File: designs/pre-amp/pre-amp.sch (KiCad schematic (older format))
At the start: 27 parts, among them J1 Conn_Coaxial, J2 Conn_01x03, J3 Conn_Coaxial, U1 AD8429, U2 OPA211

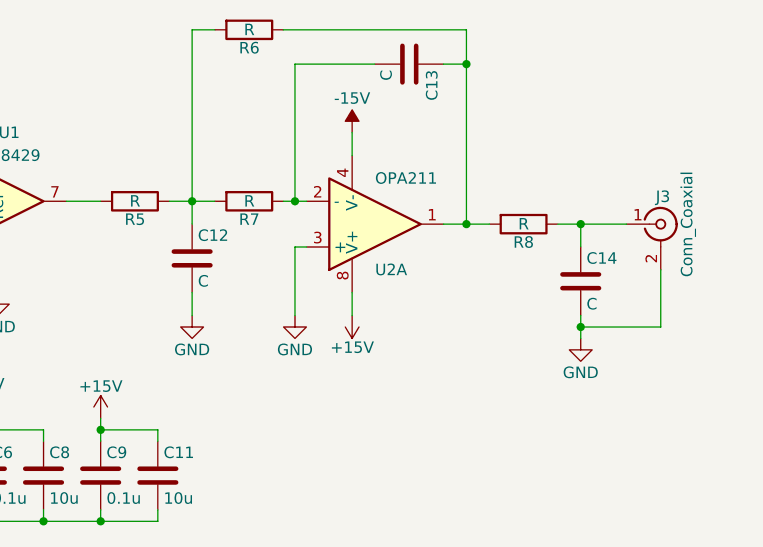
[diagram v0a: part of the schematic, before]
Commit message: [designs/pre-amp] layout
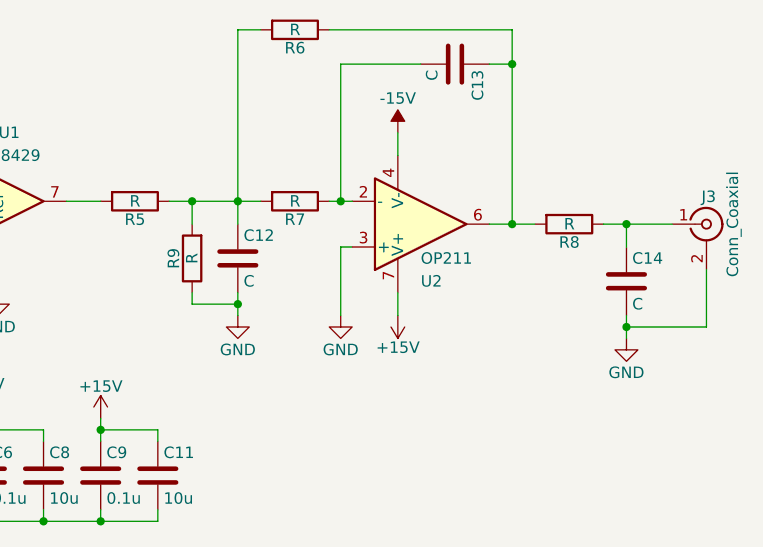
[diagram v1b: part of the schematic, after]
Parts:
- removed U2: OPA211, Housings_SOIC:SOIC-8_3.9x4.9mm_Pitch1.27mm, symbol OPA2134
- added R9: R, Resistors_SMD:R_0603, symbol R
- added U2: OP211, Housings_SOIC:SOIC-8_3.9x4.9mm_Pitch1.27mm, symbol OP179GS
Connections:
- net +15V: now also U2.7 (V+)
- net -15V: now also U2.4 (V-)
- net GND: now also R9.1, U2.3 (+)
- net at C12.1, R5.1, R6.2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: now also R9.2
- net at C13.2, R7.1: now also U2.2 (-)
- net at C13.1, R6.1, R8.2: now also U2.6
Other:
- moved on the sheet: C12, C13, C14, J3, R6, R7, R8

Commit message: [designs/pre-amp] value selections
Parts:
- C14: value C -> 0
- R8: value R -> 0
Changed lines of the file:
@@
 P 5000 1600
 F 0 "R8" V 5080 1600 50  0000 C CNN
-F 1 "R" V 5000 1600 50  0000 C CNN
+F 1 "0" V 5000 1600 50  0000 C CNN
 F 2 "Resistors_SMD:R_0603" V 4930 1600 50  0001 C CNN
 F 3 "" H 5000 1600 50  0001 C CNN
@@
 P 5250 1850
 F 0 "C14" H 5275 1950 50  0000 L CNN
-F 1 "C" H 5275 1750 50  0000 L CNN
+F 1 "0" H 5275 1750 50  0000 L CNN
 F 2 "Capacitors_SMD:C_0603" H 5288 1700 50  0001 C CNN
 F 3 "" H 5250 1850 50  0001 C CNN

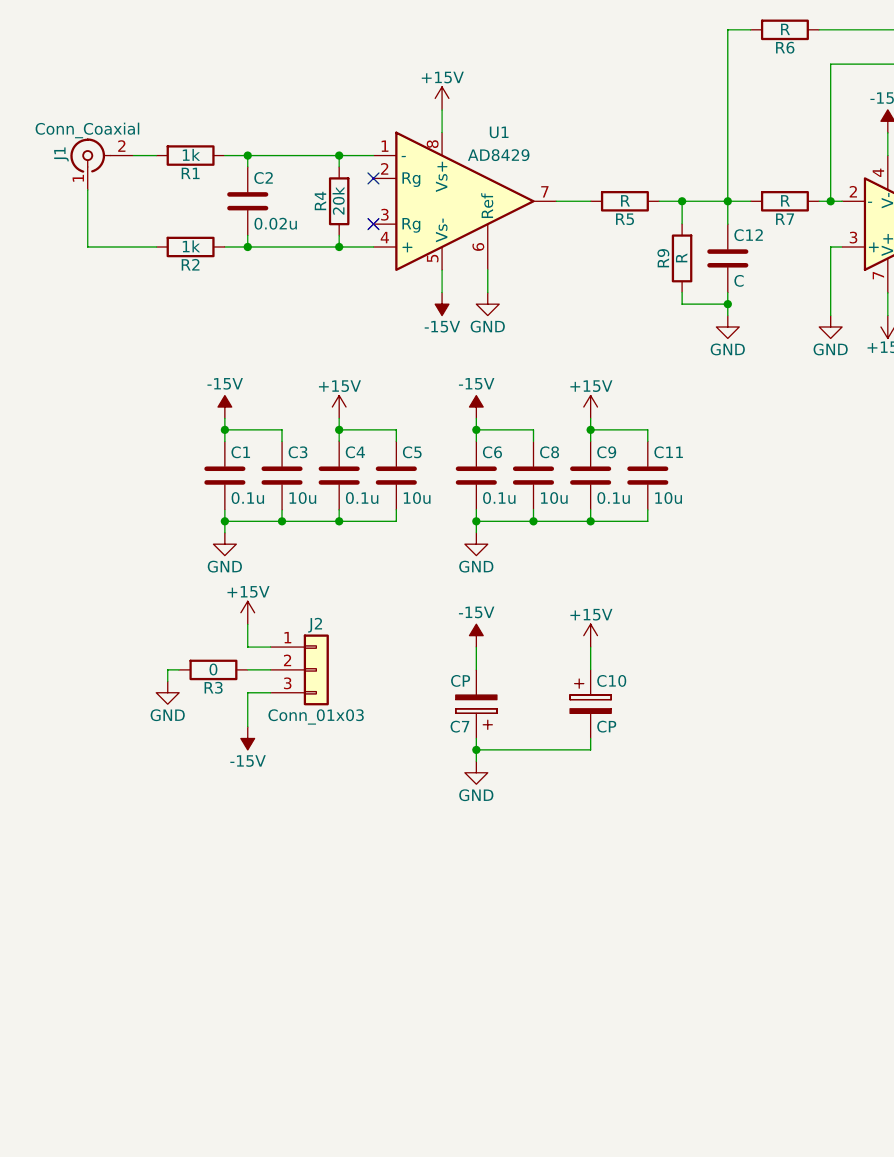
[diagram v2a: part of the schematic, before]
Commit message: [designs/pre-amp] new layout
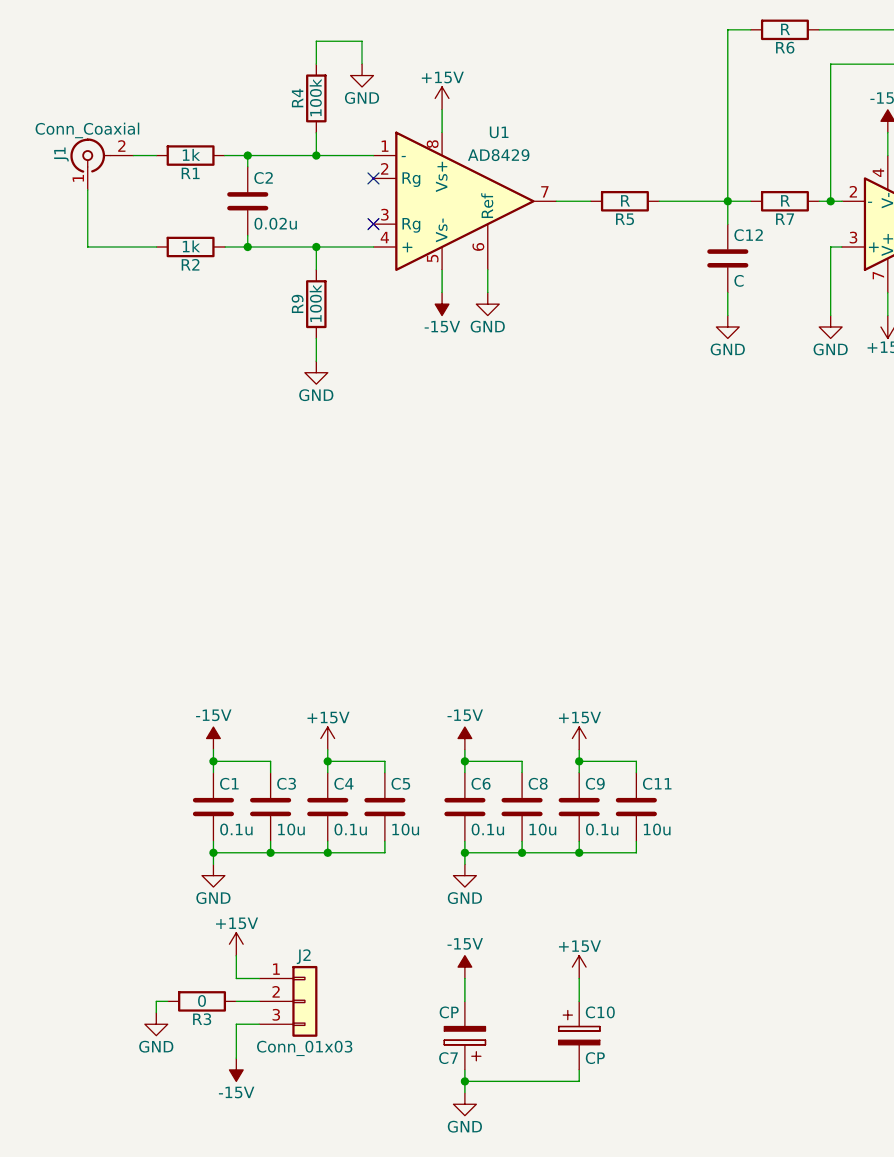
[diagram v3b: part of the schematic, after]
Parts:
- J1, J3: footprint Connectors_TE-Connectivity:BNC_Socket_TYCO-AMP_LargePads -> Connectors2:BNC_Socket_Right-Angle_LargePads
- R4: value 20k -> 100k
- R9: value R -> 100k
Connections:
- net GND: now also R4.2
- net at C2.1, R1.1, U1.1 (-): now also R4.1; no longer R4.2
- net at C2.2, R2.1, U1.4 (+): now also R9.2; no longer R4.1
- net at C12.1, R5.1, R6.2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: no longer R9.2
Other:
- moved on the sheet: C1, C10, C11, C3, C4, C5, C6, C7, C8, C9, J2, R3

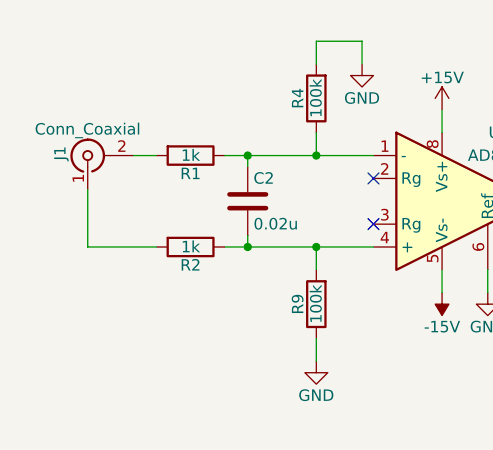
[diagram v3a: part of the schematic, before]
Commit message: [designs/pre-amp] flip input and tweak connection near the edges
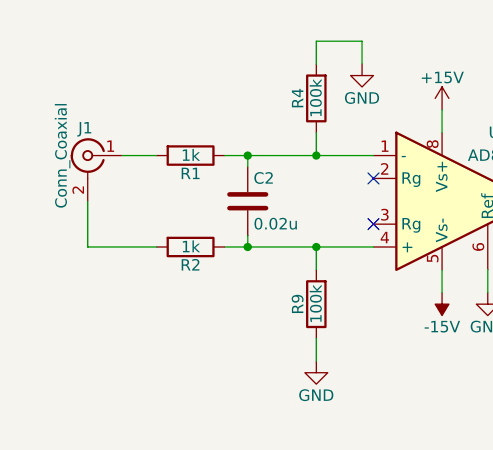
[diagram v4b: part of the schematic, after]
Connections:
- net at J1.1 (In): now also R1.2; no longer R2.2
- net at J1.2 (Ext): now also R2.2; no longer R1.2
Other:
- moved on the sheet: J1
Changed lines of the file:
@@
 F 3 "" H 750 1300 50  0001 C CNN
 	1    750  1300
-	0    -1   -1   0
+	-1   0    0    -1
 $EndComp
 $Comp
@@
 $EndComp
 Wire Wire Line
-	750  1450 750  1700
-Wire Wire Line
 	750  1700 1050 1700
-Wire Wire Line
-	950  1300 1050 1300
 Wire Wire Line
 	1350 1300 2000 1300
@@
 Wire Wire Line
 	1950 800  1950 900
+Wire Wire Line
+	900  1300 1050 1300
+Wire Wire Line
+	750  1500 750  1700
 $EndSCHEMATC

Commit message: [designs/pre-amp] move label location and update values
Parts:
- C2: value 0.02u -> 2200p
- R1, R2: value 1k -> 1.01k
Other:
- moved on the sheet: C1, C10, C11, C12, C13, C14, C2, C3, C4, C5, C6, C7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
